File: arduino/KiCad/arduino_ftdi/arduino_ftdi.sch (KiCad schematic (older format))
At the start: 19 parts, among them J1 RJ45, J10 9V-12V, J11 3V3 & 5V, J12 9V-12V, J13 3V3 & 5V, J2 IN/OUT, J3 DTR/TX/RX, J4 Power output 3V3, J5 NC, J6 DTR-FTDI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

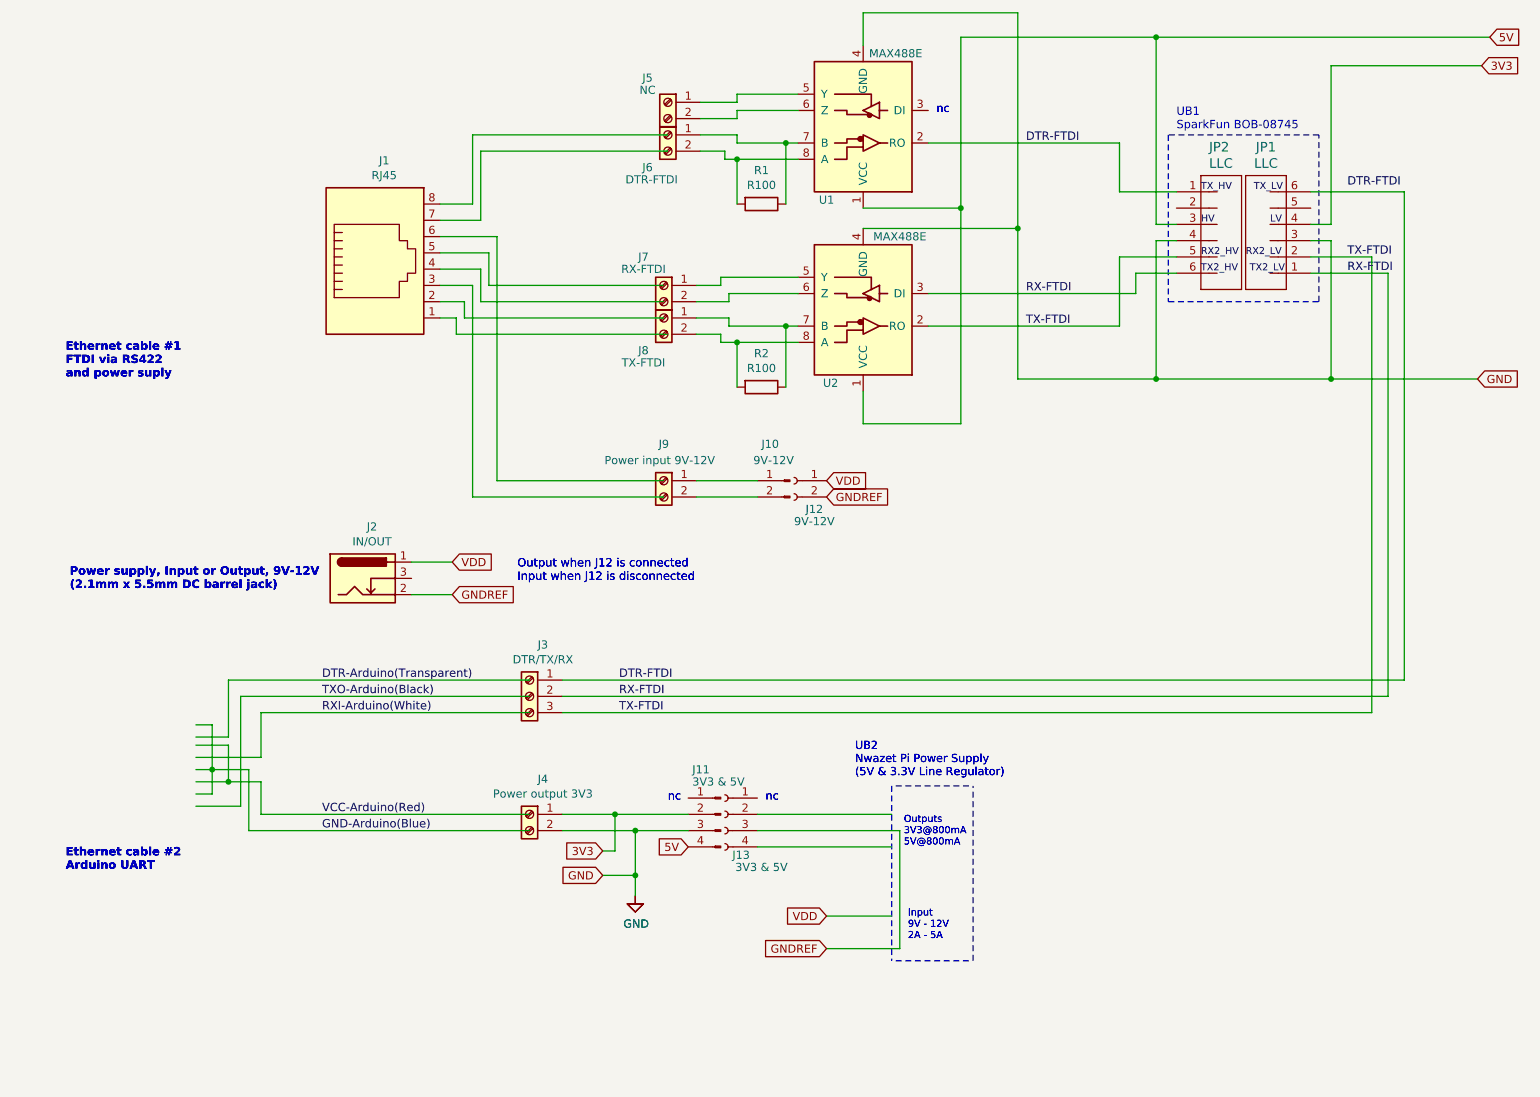
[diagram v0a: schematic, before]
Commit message: Update schematics: new connectors
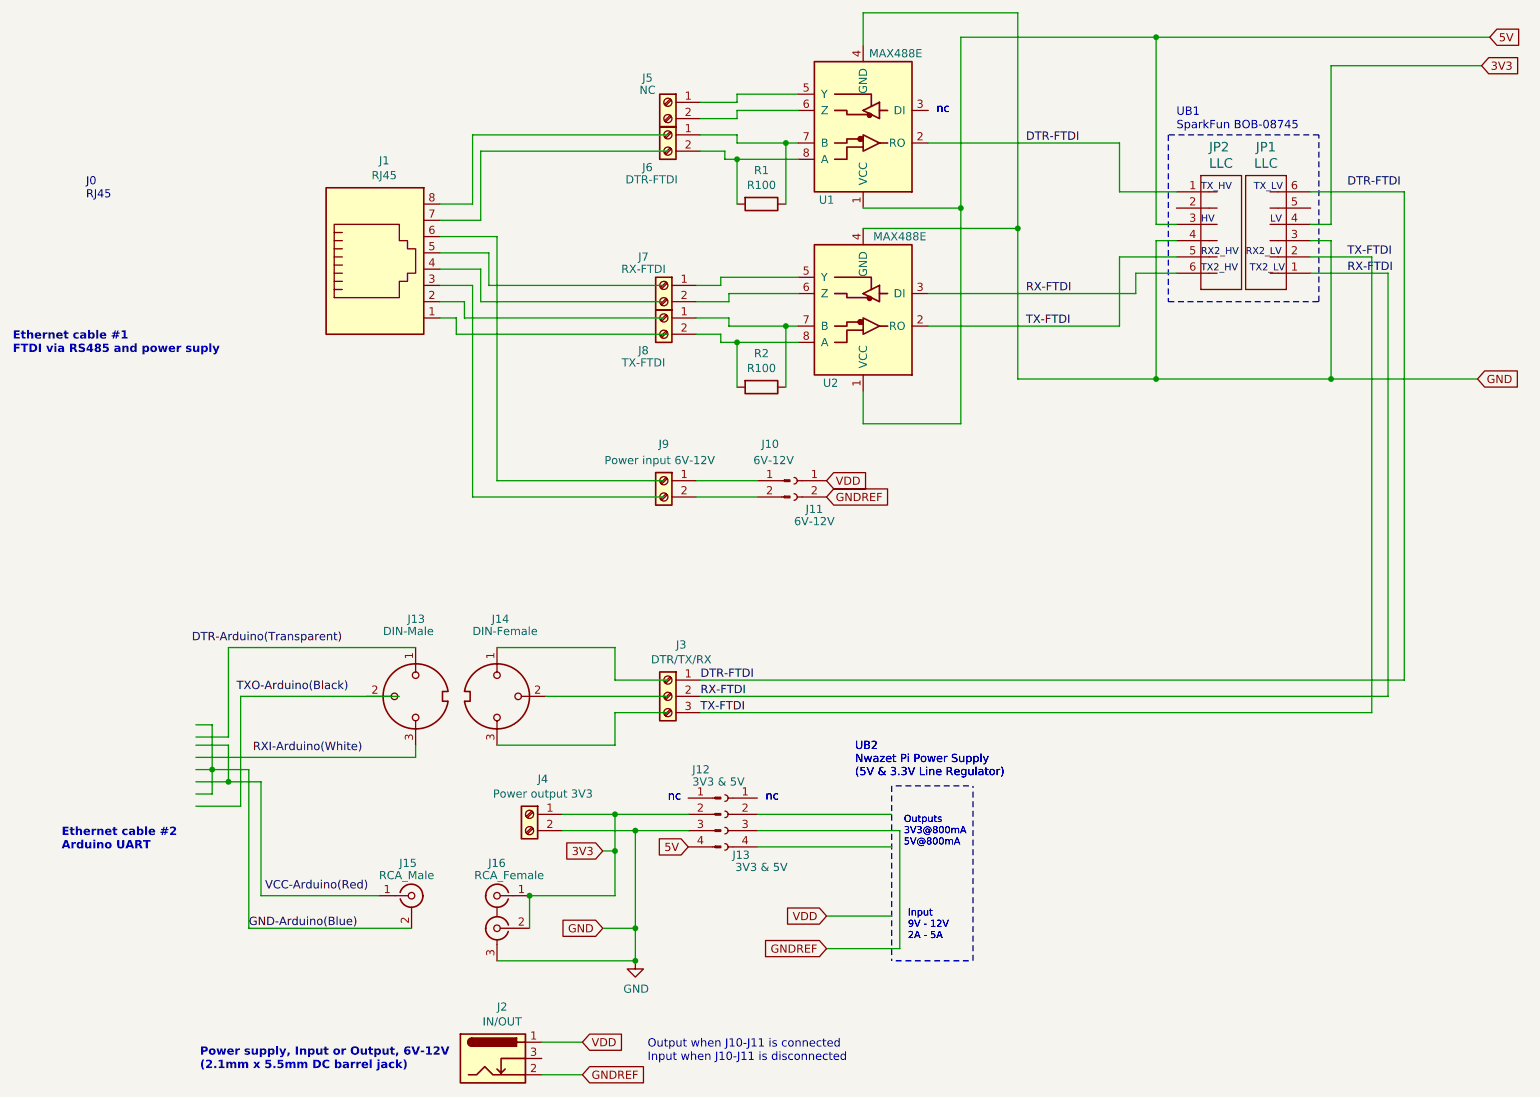
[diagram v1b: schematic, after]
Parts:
- added J13: DIN-Male, symbol Connector:DIN-3
- added J14: DIN-Female, symbol Connector:DIN-3
- added J15: RCA_Male, symbol Connector:Conn_Coaxial
- added J16: RCA_Female, symbol Connector:Conn_Coaxial_x2
- J10: value 9V-12V -> 6V-12V
- J11: renamed from J12; value 9V-12V -> 6V-12V
- J9: value Power input 9V-12V -> Power input 6V-12V
- renumbered J11 to J12
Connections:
- wire segments 140 -> 150
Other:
- note added: "Ethernet cable #1\nFTDI via RS485 and power suply"
- note added: "J0\nRJ45"
- note added: "Output when J10-J11 is connected\nInput when J10-J11 is disconnected"
- note added: "Power supply, Input or Output, 6V-12V\n(2.1mm x 5.5mm DC barrel jack)"
- note removed: "Ethernet cable #1\nFTDI via RS422 \nand power suply"
- note removed: "Output when J12 is connected\nInput when J12 is disconnected"
- note removed: "Power supply, Input or Output, 9V-12V\n(2.1mm x 5.5mm DC barrel jack)"
- moved on the sheet: J2, J3
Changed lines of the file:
@@
 Sheet 1 1
 Title "RS485 5V to UART 3V3 interface"
-Date "2021-08-21"
-Rev "3.0"
+Date "2021-09-11"
+Rev "3.5"
 Comp ""
 Comment1 "Interface to provide UART from RS485 on Ethernet cable"
@@
 L Connector:Barrel_Jack_Switch J2
 U 1 1 5F5EE7AE
-P 2950 4350
-F 0 "J2" H 3007 4667 50  0000 C CNN
-F 1 "IN/OUT" H 3007 4576 50  0000 C CNN
-F 2 "" H 3000 4310 50  0001 C CNN
-F 3 "~" H 3000 4310 50  0001 C CNN
-	1    2950 4350
+P 3750 7300
+F 0 "J2" H 3807 7617 50  0000 C CNN
+F 1 "IN/OUT" H 3807 7526 50  0000 C CNN
+F 2 "" H 3800 7260 50  0001 C CNN
+F 3 "~" H 3800 7260 50  0001 C CNN
+	1    3750 7300
 	1    0    0    -1
 $EndComp
@@
 L Connector:Screw_Terminal_01x03 J3
 U 1 1 5F62DFE4
-P 3975 5075
-F 0 "J3" H 3893 5392 50  0000 C CNN
-F 1 "DTR/TX/RX" H 3893 5301 50  0000 C CNN
-F 2 "" H 3975 5075 50  0001 C CNN
-F 3 "~" H 3975 5075 50  0001 C CNN
-	1    3975 5075
+P 4825 5075
+F 0 "J3" H 4743 5392 50  0000 C CNN
+F 1 "DTR/TX/RX" H 4743 5301 50  0000 C CNN
+F 2 "" H 4825 5075 50  0001 C CNN
+F 3 "~" H 4825 5075 50  0001 C CNN
+	1    4825 5075
 	-1   0    0    -1
 $EndComp
@@
 P 4800 3750
 F 0 "J9" H 4800 3975 50  0000 C CNN
-F 1 "Power input 9V-12V" H 4825 3875 50  0000 C CNN
+F 1 "Power input 6V-12V" H 4825 3875 50  0000 C CNN
 F 2 "" H 4800 3750 50  0001 C CNN
 F 3 "~" H 4800 3750 50  0001 C CNN
@@
 P 5575 3750
 F 0 "J10" H 5750 3975 50  0000 R CNN
-F 1 "9V-12V" H 5800 3875 50  0000 R CNN
+F 1 "6V-12V" H 5800 3875 50  0000 R CNN
 F 2 "" H 5575 3750 50  0001 C CNN
 F 3 "~" H 5575 3750 50  0001 C CNN
@@
 $EndComp
 $Comp
-L Connector:Conn_01x04_Male J11
+L Connector:Conn_01x04_Male J12
 U 1 1 5F62DFEC
 P 5150 5800
-F 0 "J11" H 5325 6075 50  0000 R CNN
+F 0 "J12" H 5325 6075 50  0000 R CNN
 F 1 "3V3 & 5V" H 5325 6000 50  0000 R CNN
 F 2 "" H 5150 5800 50  0001 C CNN
@@
 	4175 5900 4625 5900
 $Comp
-L Connector:Conn_01x02_Female J12
+L Connector:Conn_01x02_Female J11
 U 1 1 5F62DFED
 P 5600 3750
-F 0 "J12" H 5475 3575 50  0000 C CNN
-F 1 "9V-12V" H 5475 3500 50  0000 C CNN
+F 0 "J11" H 5475 3575 50  0000 C CNN
+F 1 "6V-12V" H 5475 3500 50  0000 C CNN
 F 2 "" H 5600 3750 50  0001 C CNN
 F 3 "~" H 5600 3750 50  0001 C CNN
@@
 Text GLabel 5800 3850 2    50   Input ~ 0
 GNDREF
-Text GLabel 4425 6175 0    50   Input ~ 0
+Text GLabel 4425 6500 0    50   Input ~ 0
 GND
-Text GLabel 3500 4450 2    50   Input ~ 0
+Text GLabel 4300 7400 2    50   Input ~ 0
 GNDREF
 Wire Wire Line
-	3500 4250 3250 4250
+	4300 7200 4050 7200
 Text GLabel 9875 1025 2    50   Input ~ 0
 5V
@@
 Text Notes 6300 6575 0    43   ~ 0
 Input\n9V - 12V\n2A - 5A
-Text Notes 1125 6150 0    51   ~ 10
-Ethernet cable #2\nArduino UART
-Text Notes 1125 3125 0    51   ~ 10
-Ethernet cable #1\nFTDI via RS422 \nand power suply
-Text Notes 1150 4425 0    51   ~ 10
-Power supply, Input or Output, 9V-12V\n(2.1mm x 5.5mm DC barrel jack)
-Text Notes 3900 4375 0    51   ~ 0
-Output when J12 is connected\nInput when J12 is disconnected
 Wire Wire Line
-	3500 4450 3250 4450
+	4300 7400 4050 7400
 Wire Wire Line
 	5000 3850 5375 3850
@@
 Wire Wire Line
 	6250 6625 6250 5900
-$Comp
-L power:GND #PWR?
-U 1 1 5F62DFF2
-P 4625 6300
-F 0 "#PWR?" H 4625 6050 50  0001 C CNN
-F 1 "GND" H 4630 6127 50  0000 C CNN
-F 2 "" H 4625 6300 50  0001 C CNN
-F 3 "" H 4625 6300 50  0001 C CNN
-	1    4625 6300
-	1    0    0    -1
-$EndComp
 Wire Wire Line
 	5800 6425 6200 6425
@@
 	4500 5800 4950 5800
 Wire Wire Line
-	4425 6175 4625 6175
+	4425 6500 4625 6500
 Connection ~ 4625 5900
 Wire Wire Line
@@
 	5800 6625 6250 6625
 Wire Wire Line
-	4625 5900 4625 6175
-Connection ~ 4625 6175
-Wire Wire Line
-	4625 6175 4625 6300
+	4625 5900 4625 6500
 Wire Wire Line
 	8900 2175 8900 1200
@@
 	9350 1975 9350 4975
 Wire Wire Line
-	4175 4975 9350 4975
+	5025 4975 9350 4975
 Wire Wire Line
-	4175 5075 9250 5075
+	5025 5075 9250 5075
 Wire Wire Line
 	1925 5250 2025 5250
@@
 	2125 5375 2125 5600
 Wire Wire Line
-	3975 5900 2250 5900
-Wire Wire Line
-	2250 5900 2250 5525
+	2250 6500 2250 5525
 Wire Wire Line
 	2250 5525 2025 5525
@@
 	2125 5600 2325 5600
 Wire Wire Line
-	2325 5600 2325 5800
+	2325 5600 2325 6300
 Wire Wire Line
-	2325 5800 3975 5800
+	2325 6300 3050 6300
 Connection ~ 2125 5600
-Text Label 2700 5800 0    51   ~ 0
+Text Label 2350 6275 0    51   ~ 0
 VCC-Arduino(Red)
 Wire Wire Line
-	1925 5450 2325 5450
-Wire Wire Line
-	2325 5450 2325 5175
-Wire Wire Line
-	2325 5175 3975 5175
-Wire Wire Line
 	1925 5750 2200 5750
 Wire Wire Line
 	2200 5750 2200 5075
 Wire Wire Line
-	2200 5075 3975 5075
-Wire Wire Line
 	1925 5325 2125 5325
 Wire Wire Line
-	2125 5325 2125 4975
+	2125 5325 2125 4775
 Wire Wire Line
-	2125 4975 3975 4975
-Text Label 2700 4975 0    51   ~ 0
+	2125 4775 3275 4775
+Text Label 1900 4750 0    51   ~ 0
 DTR-Arduino(Transparent)
-Text Label 2700 5075 0    51   ~ 0
+Text Label 2175 5050 0    51   ~ 0
 TXO-Arduino(Black)
-Text Label 4525 5175 0    51   ~ 0
+Text Label 5025 5175 0    51   ~ 0
 TX-FTDI
 $Comp
@@
 Text GLabel 4425 6025 0    50   Input ~ 0
 3V3
-Text GLabel 3500 4250 2    50   Input ~ 0
+Text GLabel 4300 7200 2    50   Input ~ 0
 VDD
 Text GLabel 9825 1200 2    50   Input ~ 0
@@
 Text Notes 6300 6575 0    43   ~ 0
 Input\n9V - 12V\n2A - 5A
-Text Notes 1125 6150 0    51   ~ 10
+Text Notes 1100 6025 0    51   ~ 10
 Ethernet cable #2\nArduino UART
-Text Notes 1125 3125 0    51   ~ 10
-Ethernet cable #1\nFTDI via RS422 \nand power suply
-Text Notes 1150 4425 0    51   ~ 10
-Power supply, Input or Output, 9V-12V\n(2.1mm x 5.5mm DC barrel jack)
-Text Notes 3900 4375 0    51   ~ 0
-Output when J12 is connected\nInput when J12 is disconnected
+Text Notes 800  2975 0    51   ~ 10
+Ethernet cable #1\nFTDI via RS485 and power suply
+Text Notes 1950 7375 0    51   ~ 10
+Power supply, Input or Output, 6V-12V\n(2.1mm x 5.5mm DC barrel jack)
+Text Notes 4700 7325 0    51   ~ 0
+Output when J10-J11 is connected\nInput when J10-J11 is disconnected
 $Comp
 L power:GND #PWR?
 U 1 1 5F653183
-P 4625 6300
-F 0 "#PWR?" H 4625 6050 50  0001 C CNN
-F 1 "GND" H 4630 6127 50  0000 C CNN
-F 2 "" H 4625 6300 50  0001 C CNN
-F 3 "" H 4625 6300 50  0001 C CNN
-	1    4625 6300
+P 4625 6700
+F 0 "#PWR?" H 4625 6450 50  0001 C CNN
+F 1 "GND" H 4630 6527 50  0000 C CNN
+F 2 "" H 4625 6700 50  0001 C CNN
+F 3 "" H 4625 6700 50  0001 C CNN
+	1    4625 6700
 	1    0    0    -1
 $EndComp
@@
 EndData
 $EndBitmap
-Text Label 2700 5175 0    51   ~ 0
+Text Label 2275 5425 0    51   ~ 0
 RXI-Arduino(White)
-Text Label 4525 5075 0    51   ~ 0
+Text Label 5025 5075 0    51   ~ 0
 RX-FTDI
-Text Label 4525 4975 0    51   ~ 0
+Text Label 5025 4975 0    51   ~ 0
 DTR-FTDI
 Text Notes 6475 1500 0    50   ~ 0
@@
 UB1\nSparkFun BOB-08745
 Wire Wire Line
-	4175 5175 9150 5175
+	5025 5175 9150 5175
 Wire Wire Line
 	9250 2475 9250 5075
@@
 Text Label 9000 2375 0    51   ~ 0
 TX-FTDI
-Text Label 2700 5900 0    51   ~ 0
+Text Label 2250 6500 0    51   ~ 0
 GND-Arduino(Blue)
+$Comp
+L Connector:DIN-3 J14
+U 1 1 613D692C
+P 3775 5075
+F 0 "J14" V 3300 5150 50  0000 R CNN
+F 1 "DIN-Female" V 3375 5325 50  0000 R CNN
+F 2 "" H 3775 5075 50  0001 C CNN
+F 3 "http://www.mouser.com/ds/2/18/40_c091_abd_e-75918.pdf" H 3775 5075 50  0001 C CNN
+	1    3775 5075
+	0    1    1    0
+$EndComp
+Wire Wire Line
+	3775 4775 4500 4775
+Wire Wire Line
+	4500 4775 4500 4975
+Wire Wire Line
+	4500 4975 4825 4975
+Wire Wire Line
+	4075 5075 4825 5075
+Wire Wire Line
+	3775 5375 4500 5375
+Wire Wire Line
+	4500 5375 4500 5175
+Wire Wire Line
+	4500 5175 4825 5175
+$Comp
+L Connector:Conn_Coaxial_x2 J16
+U 1 1 6142E3E5
+P 3775 6400
+F 0 "J16" H 3775 6700 50  0000 C CNN
+F 1 "RCA_Female" H 3700 6625 50  0000 C CNN
+F 2 "" H 3775 6300 50  0001 C CNN
+F 3 " ~" H 3775 6300 50  0001 C CNN
+	1    3775 6400
+	-1   0    0    -1
+$EndComp
+Wire Wire Line
+	3775 6700 4625 6700
+Connection ~ 4625 6700
+Wire Wire Line
+	4625 6500 4625 6700
+Connection ~ 4625 6500
+Wire Wire Line
+	4500 6025 4500 6300
+Wire Wire Line
+	4500 6300 3975 6300
+Connection ~ 4500 6025
+Wire Wire Line
+	3975 6300 3975 6500
+Connection ~ 3975 6300
+$Comp
+L Connector:Conn_Coaxial J15
+U 1 1 614D0481
+P 3250 6300
+F 0 "J15" H 3175 6500 50  0000 L CNN
+F 1 "RCA_Male" H 3050 6425 50  0000 L CNN
+F 2 "" H 3250 6300 50  0001 C CNN
+F 3 " ~" H 3250 6300 50  0001 C CNN
+	1    3250 6300
+	1    0    0    -1
+$EndComp
+Wire Wire Line
+	2250 6500 3250 6500
+$Comp
+L Connector:DIN-3 J13
+U 1 1 614F0ACC
+P 3275 5075
+F 0 "J13" V 2800 5125 50  0000 R CNN
+F 1 "DIN-Male" V 2875 5275 50  0000 R CNN
+F 2 "" H 3275 5075 50  0001 C CNN
+F 3 "http://www.mouser.com/ds/2/18/40_c091_abd_e-75918.pdf" H 3275 5075 50  0001 C CNN
+	1    3275 5075
+	0    -1   1    0
+$EndComp
+Wire Wire Line
+	2200 5075 3175 5075
+Wire Wire Line
+	1925 5450 3275 5450
+Wire Wire Line
+	3275 5450 3275 5375
+Text Notes 1250 2025 0    50   ~ 0
+J0\nRJ45
 $EndSCHEMATC
